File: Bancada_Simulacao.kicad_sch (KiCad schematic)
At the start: 2 parts

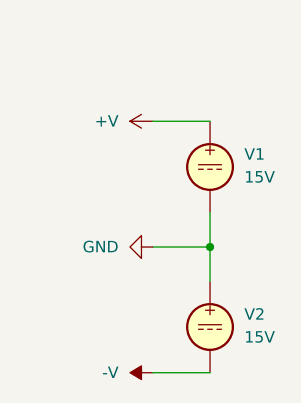
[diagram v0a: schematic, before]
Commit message: Valida cascata subbass 40 Hz e subsonico 10 Hz em ±15 V
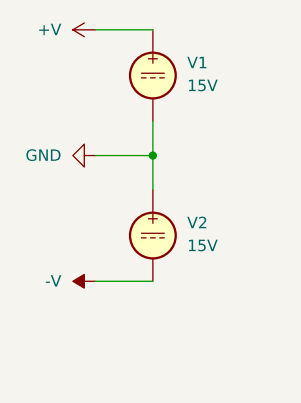
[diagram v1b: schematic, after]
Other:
- moved on the sheet: V1, V2
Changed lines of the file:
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@@
 	)
 	(junction
-		(at 149.86 110.49)
+		(at 143.51 100.33)
 		(diameter 0)
 		(color 0 0 0 0)
@@
 	(wire
 		(pts
-			(xy 143.51 96.52) (xy 149.86 96.52)
+			(xy 137.16 86.36) (xy 143.51 86.36)
 		)
 		(stroke
@@
 	(wire
 		(pts
-			(xy 149.86 110.49) (xy 149.86 114.3)
+			(xy 143.51 100.33) (xy 143.51 104.14)
 		)
 		(stroke
@@
 	(wire
 		(pts
-			(xy 143.51 124.46) (xy 149.86 124.46)
+			(xy 137.16 114.3) (xy 143.51 114.3)
 		)
 		(stroke
@@
 	(wire
 		(pts
-			(xy 143.51 110.49) (xy 149.86 110.49)
+			(xy 137.16 100.33) (xy 143.51 100.33)
 		)
 		(stroke
@@
 	(wire
 		(pts
-			(xy 149.86 106.68) (xy 149.86 110.49)
+			(xy 143.51 96.52) (xy 143.51 100.33)
 		)
 		(stroke
@@
 	(symbol
 		(lib_id "Simulation_SPICE:VDC")
-		(at 149.86 119.38 0)
+		(at 143.51 109.22 0)
 		(unit 1)
 		(body_style 1)
@@
 		(fields_autoplaced yes)
 		(property "Reference" "V2"
-			(at 153.67 117.9801 0)
+			(at 147.32 107.8201 0)
 			(show_name no)
 			(do_not_autoplace no)
@@
 		)
 		(property "Value" "15V"
-			(at 153.67 120.5201 0)
+			(at 147.32 110.3601 0)
 			(show_name no)
 			(do_not_autoplace no)
@@
 		)
 		(property "Footprint" ""
-			(at 149.86 119.38 0)
+			(at 143.51 109.22 0)
 			(hide yes)
 			(show_name no)
@@
 		)
 		(property "Datasheet" "https://ngspice.sourceforge.io/docs/ngspice-html-manual/manual.xhtml#sec_Independent_Sources_for"
-			(at 149.86 119.38 0)
+			(at 143.51 109.22 0)
 			(hide yes)
 			(show_name no)
@@
 		)
 		(property "Description" "Voltage source, DC"
-			(at 149.86 119.38 0)
+			(at 143.51 109.22 0)
 			(hide yes)
 			(show_name no)
@@
 		)
 		(property "Sim.Pins" "1=+ 2=-"
-			(at 149.86 119.38 0)
+			(at 143.51 109.22 0)
 			(hide yes)
 			(show_name no)
@@
 		)
 		(property "Sim.Type" "DC"
-			(at 149.86 119.38 0)
+			(at 143.51 109.22 0)
 			(hide yes)
 			(show_name no)
@@
 		)
 		(property "Sim.Device" "V"
-			(at 149.86 119.38 0)
+			(at 143.51 109.22 0)
 			(hide yes)
 			(show_name no)
@@
 	(symbol
 		(lib_id "power:+15V")
-		(at 143.51 96.52 90)
+		(at 137.16 86.36 90)
 		(unit 1)
 		(body_style 1)
@@
 		(fields_autoplaced yes)
 		(property "Reference" "#PWR05"
-			(at 147.32 96.52 0)
+			(at 140.97 86.36 0)
 			(hide yes)
 			(show_name no)
@@
 		)
 		(property "Value" "+V"
-			(at 139.7 96.5199 90)
+			(at 133.35 86.3599 90)
 			(show_name no)
 			(do_not_autoplace no)
@@
 		)
 		(property "Footprint" ""
-			(at 143.51 96.52 0)
+			(at 137.16 86.36 0)
 			(hide yes)
 			(show_name no)
@@
 		)
 		(property "Datasheet" ""
-			(at 143.51 96.52 0)
+			(at 137.16 86.36 0)
 			(hide yes)
 			(show_name no)
@@
 		)
 		(property "Description" "Power symbol creates a global label with name \"+15V\""
-			(at 143.51 96.52 0)
+			(at 137.16 86.36 0)
 			(hide yes)
 			(show_name no)
@@
 	(symbol
 		(lib_id "power:-15V")
-		(at 143.51 124.46 90)
+		(at 137.16 114.3 90)
 		(unit 1)
 		(body_style 1)
@@
 		(fields_autoplaced yes)
 		(property "Reference" "#PWR06"
-			(at 147.32 124.46 0)
+			(at 140.97 114.3 0)
 			(hide yes)
 			(show_name no)
@@
 		)
 		(property "Value" "-V"
-			(at 139.7 124.4599 90)
+			(at 133.35 114.2999 90)
 			(show_name no)
 			(do_not_autoplace no)
@@
 		)
 		(property "Footprint" ""
-			(at 143.51 124.46 0)
+			(at 137.16 114.3 0)
 			(hide yes)
 			(show_name no)
@@
 		)
 		(property "Datasheet" ""
-			(at 143.51 124.46 0)
+			(at 137.16 114.3 0)
 			(hide yes)
 			(show_name no)
@@
 		)
 		(property "Description" "Power symbol creates a global label with name \"-15V\""
-			(at 143.51 124.46 0)
+			(at 137.16 114.3 0)
 			(hide yes)
 			(show_name no)
@@
 	(symbol
 		(lib_id "power:GND")
-		(at 143.51 110.49 270)
+		(at 137.16 100.33 270)
 		(unit 1)
 		(body_style 1)
@@
 		(fields_autoplaced yes)
 		(property "Reference" "#PWR04"
-			(at 137.16 110.49 0)
+			(at 130.81 100.33 0)
 			(hide yes)
 			(show_name no)
@@
 		)
 		(property "Value" "GND"
-			(at 139.7 110.4899 90)
+			(at 133.35 100.3299 90)
 			(show_name no)
 			(do_not_autoplace no)
@@
 		)
 		(property "Footprint" ""
-			(at 143.51 110.49 0)
+			(at 137.16 100.33 0)
 			(hide yes)
 			(show_name no)
@@
 		)
 		(property "Datasheet" ""
-			(at 143.51 110.49 0)
+			(at 137.16 100.33 0)
 			(hide yes)
 			(show_name no)
@@
 		)
 		(property "Description" "Power symbol creates a global label with name \"GND\" , ground"
-			(at 143.51 110.49 0)
+			(at 137.16 100.33 0)
 			(hide yes)
 			(show_name no)
@@
 	(symbol
 		(lib_id "Simulation_SPICE:VDC")
-		(at 149.86 101.6 0)
+		(at 143.51 91.44 0)
 		(unit 1)
 		(body_style 1)
@@
 		(fields_autoplaced yes)
 		(property "Reference" "V1"
-			(at 153.67 100.2001 0)
+			(at 147.32 90.0401 0)
 			(show_name no)
 			(do_not_autoplace no)
@@
 		)
 		(property "Value" "15V"
-			(at 153.67 102.7401 0)
+			(at 147.32 92.5801 0)
 			(show_name no)
 			(do_not_autoplace no)
@@
 		)
 		(property "Footprint" ""
-			(at 149.86 101.6 0)
+			(at 143.51 91.44 0)
 			(hide yes)
 			(show_name no)
@@
 		)
 		(property "Datasheet" "https://ngspice.sourceforge.io/docs/ngspice-html-manual/manual.xhtml#sec_Independent_Sources_for"
-			(at 149.86 101.6 0)
+			(at 143.51 91.44 0)
 			(hide yes)
 			(show_name no)
@@
 		)
 		(property "Description" "Voltage source, DC"
-			(at 149.86 101.6 0)
+			(at 143.51 91.44 0)
 			(hide yes)
 			(show_name no)
@@
 		)
 		(property "Sim.Pins" "1=+ 2=-"
-			(at 149.86 101.6 0)
+			(at 143.51 91.44 0)
 			(hide yes)
 			(show_name no)
@@
 		)
 		(property "Sim.Type" "DC"
-			(at 149.86 101.6 0)
+			(at 143.51 91.44 0)
 			(hide yes)
 			(show_name no)
@@
 		)
 		(property "Sim.Device" "V"
-			(at 149.86 101.6 0)
-			(hide yes)
-			(show_name no)
+			(at 143.51 91.44 0)
+			(hide yes)
+			(show_name no)

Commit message: Conclui ensaios de degrau e sequenciamento da alimentacao do subbass
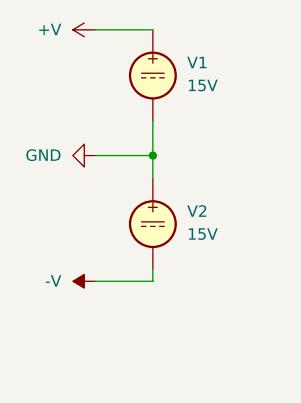
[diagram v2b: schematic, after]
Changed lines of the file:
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@@
 	(wire
 		(pts
-			(xy 143.51 100.33) (xy 143.51 104.14)
+			(xy 137.16 114.3) (xy 143.51 114.3)
 		)
 		(stroke
@@
 	(wire
 		(pts
-			(xy 137.16 114.3) (xy 143.51 114.3)
+			(xy 143.51 114.3) (xy 143.51 113.03)
 		)
 		(stroke
@@
 	(wire
 		(pts
-			(xy 137.16 100.33) (xy 143.51 100.33)
+			(xy 143.51 100.33) (xy 143.51 102.87)
 		)
 		(stroke
@@
 	(wire
 		(pts
-			(xy 143.51 96.52) (xy 143.51 100.33)
+			(xy 137.16 100.33) (xy 143.51 100.33)
 		)
 		(stroke
@@
 		)
 	)
+	(wire
+		(pts
+			(xy 143.51 96.52) (xy 143.51 100.33)
+		)
+		(stroke
+			(width 0)
+			(type default)
+		)
+	)
 	(symbol
 		(lib_id "Simulation_SPICE:VDC")
-		(at 143.51 109.22 0)
+		(at 143.51 107.95 0)
 		(unit 1)
 		(body_style 1)
@@
 		(fields_autoplaced yes)
 		(property "Reference" "V2"
-			(at 147.32 107.8201 0)
+			(at 147.32 106.5501 0)
 			(show_name no)
 			(do_not_autoplace no)
@@
 		)
 		(property "Value" "15V"
-			(at 147.32 110.3601 0)
+			(at 147.32 109.0901 0)
 			(show_name no)
 			(do_not_autoplace no)
@@
 		)
 		(property "Footprint" ""
-			(at 143.51 109.22 0)
+			(at 143.51 107.95 0)
 			(hide yes)
 			(show_name no)
@@
 		)
 		(property "Datasheet" "https://ngspice.sourceforge.io/docs/ngspice-html-manual/manual.xhtml#sec_Independent_Sources_for"
-			(at 143.51 109.22 0)
+			(at 143.51 107.95 0)
 			(hide yes)
 			(show_name no)
@@
 		)
 		(property "Description" "Voltage source, DC"
-			(at 143.51 109.22 0)
+			(at 143.51 107.95 0)
 			(hide yes)
 			(show_name no)
@@
 		)
 		(property "Sim.Pins" "1=+ 2=-"
-			(at 143.51 109.22 0)
+			(at 143.51 107.95 0)
 			(hide yes)
 			(show_name no)
@@
 		)
 		(property "Sim.Type" "DC"
-			(at 143.51 109.22 0)
+			(at 143.51 107.95 0)
 			(hide yes)
 			(show_name no)
@@
 		)
 		(property "Sim.Device" "V"
-			(at 143.51 109.22 0)
-			(hide yes)
-			(show_name no)
-			(do_not_autoplace no)
-			(effects
-				(font
-					(size 1.27 1.27)
-				)
-				(justify left)
+			(at 143.51 107.95 0)
+			(hide yes)
+			(show_name no)
+			(do_not_autoplace no)
+			(effects
+				(font
+					(size 1.27 1.27)
+				)
+				(justify left)
+			)
+		)
+		(property "Sim.Params" "dc=15"
+			(at 143.51 107.95 0)
+			(hide yes)
+			(show_name no)
+			(do_not_autoplace no)
+			(effects
+				(font
+					(size 1.27 1.27)
+				)
 			)
 		)
@@
 			)
 		)
+		(property "Sim.Params" "dc=15"
+			(at 143.51 91.44 0)
+			(hide yes)
+			(show_name no)
+			(do_not_autoplace no)
+			(effects
+				(font
+					(size 1.27 1.27)
+				)
+			)
+		)

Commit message: Add SubBass mute control and verification scripts
- Introduced a new SPICE subcircuit for SubBass mute control, implementing a dual-rail supervisor with diagnostic outputs.
- Created a symbol library for Hi-Fi audio components in KiCad.
- Added a Python script to plot results from SubBass simulations, visualizing startup, shutdown, and AC response.
- Developed a verification script for the SubBass design, exporting netlists and validating functionality through simulation with ngspice.
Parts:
- V1, V2: now left out of the parts list
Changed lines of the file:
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@@
 		(body_style 1)
 		(exclude_from_sim no)
-		(in_bom yes)
-		(on_board yes)
+		(in_bom no)
+		(on_board no)
 		(in_pos_files yes)
 		(dnp no)
@@
 		(body_style 1)
 		(exclude_from_sim no)
-		(in_bom yes)
-		(on_board yes)
-		(in_pos_files yes)
-		(dnp no)
+		(in_bom no)
+		(on_board no)
+		(in_pos_files yes)
+		(dnp no)
